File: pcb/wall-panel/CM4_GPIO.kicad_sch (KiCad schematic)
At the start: 24 parts, among them J10 THD-20-R, J15 THD-20-R, J16 Micro_SD_Card_Det, J18 THD-20-R, SW1 power reset, SW2 cpu reset, U10 RT9742GGJ5, U9 74LVC1G07SE-7

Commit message: wall panel v0.3
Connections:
- net ID_SC: now also JP4.1 (A); no longer JP4.3 (B)
- net ID_SD: now also JP3.1 (A); no longer JP3.3 (B)
- net SCL3: now also JP4.3 (B); no longer JP4.1 (A)
- net SDA3: now also JP3.3 (B); no longer JP3.1 (A)
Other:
- note added: "back plate"
- note added: "ethernet"
- company: Grigorii Merkushev (aka brushknight) -> dotstar.tech
- title: Wall panel -> Wall Panel
- moved on the sheet: JP3, JP4
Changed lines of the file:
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@@
 	(paper "A3")
 	(title_block
-		(title "Wall panel")
-		(date "2026-01-09")
-		(rev "1")
-		(company "Grigorii Merkushev (aka brushknight)")
-		(comment 1 "brushknight.com")
+		(title "Wall Panel")
+		(date "2026-02-02")
+		(rev "v0.3")
+		(company "dotstar.tech")
+		(comment 1 "designed by Grigorii Merkushev (aka brushknight)")
+		(comment 2 "brushknight.com")
 	)
 	(text "PWR LED"
@@
 		)
 	)
+	(text "back plate"
+		(exclude_from_sim no)
+		(at 254 21.082 0)
+		(effects
+			(font
+				(size 1.27 1.27)
+			)
+			(justify left bottom)
+		)
+	)
+	(text "ethernet"
+		(exclude_from_sim no)
+		(at 211.582 21.59 0)
+		(effects
+			(font
+				(size 1.27 1.27)
+			)
+			(justify left bottom)
+		)
+	)
 	(junction
 		(at 37.846 92.71)
@@
 	(wire
 		(pts
-			(xy 330.2 54.61) (xy 334.01 54.61)
+			(xy 327.66 72.39) (xy 331.47 72.39)
 		)
 		(stroke
@@
 	(wire
 		(pts
-			(xy 330.2 29.21) (xy 330.2 33.02)
+			(xy 327.66 46.99) (xy 327.66 50.8)
 		)
 		(stroke
@@
 	(wire
 		(pts
-			(xy 330.2 33.02) (xy 334.01 33.02)
+			(xy 327.66 50.8) (xy 331.47 50.8)
 		)
 		(stroke
@@
 	(wire
 		(pts
-			(xy 330.2 39.37) (xy 334.01 39.37)
+			(xy 327.66 57.15) (xy 331.47 57.15)
 		)
 		(stroke
@@
 	(wire
 		(pts
-			(xy 330.2 19.05) (xy 330.2 15.24)
+			(xy 327.66 36.83) (xy 327.66 33.02)
 		)
 		(stroke
@@
 	(wire
 		(pts
-			(xy 330.2 15.24) (xy 334.01 15.24)
+			(xy 327.66 33.02) (xy 331.47 33.02)
 		)
 		(stroke
@@
 	(wire
 		(pts
-			(xy 330.2 52.07) (xy 330.2 54.61)
+			(xy 327.66 69.85) (xy 327.66 72.39)
 		)
 		(stroke
@@
 	(wire
 		(pts
-			(xy 330.2 41.91) (xy 330.2 39.37)
+			(xy 327.66 59.69) (xy 327.66 57.15)
 		)
 		(stroke
@@
 	(hierarchical_label "SCL3"
 		(shape output)
-		(at 334.01 39.37 0)
+		(at 331.47 57.15 0)
 		(effects
 			(font
@@
 	(hierarchical_label "SDA3"
 		(shape output)
-		(at 334.01 15.24 0)
+		(at 331.47 33.02 0)
 		(effects
 			(font
@@
 	(hierarchical_label "TOUCH_SDA"
 		(shape output)
-		(at 334.01 24.13 0)
+		(at 331.47 41.91 0)
 		(effects
 			(font
@@
 	(hierarchical_label "TOUCH_SCL"
 		(shape output)
-		(at 334.01 46.99 0)
+		(at 331.47 64.77 0)
 		(effects
 			(font
@@
 	(hierarchical_label "ID_SD"
 		(shape output)
-		(at 334.01 33.02 0)
+		(at 331.47 50.8 0)
 		(effects
 			(font
@@
 	(hierarchical_label "ID_SC"
 		(shape output)
-		(at 334.01 54.61 0)
+		(at 331.47 72.39 0)
 		(effects
 			(font
@@
 		)
 		(instances
-			(project "CM4IOv5"
+			(project "wall_panel"
 				(path "/e63e39d7-6ac0-4ffd-8aa3-1841a4541b55/00000000-0000-0000-0000-00005cff706a"
 					(reference "#PWR078")
@@
 		)
 		(instances
-			(project "CM4IOv5"
+			(project "wall_panel"
 				(path "/e63e39d7-6ac0-4ffd-8aa3-1841a4541b55/00000000-0000-0000-0000-00005cff706a"
 					(reference "R24")
@@
 		)
 		(instances
-			(project "CM4IOv5"
+			(project "wall_panel"
 				(path "/e63e39d7-6ac0-4ffd-8aa3-1841a4541b55/00000000-0000-0000-0000-00005cff706a"
 					(reference "#PWR071")
@@
 		)
 		(instances
-			(project "CM4IOv5"
+			(project "wall_panel"
 				(path "/e63e39d7-6ac0-4ffd-8aa3-1841a4541b55/00000000-0000-0000-0000-00005cff706a"
 					(reference "#PWR032")
@@
 		)
 		(instances
-			(project "CM4IOv5"
+			(project "wall_panel"
 				(path "/e63e39d7-6ac0-4ffd-8aa3-1841a4541b55/00000000-0000-0000-0000-00005cff706a"
 					(reference "#PWR075")
@@
 		)
 		(instances
-			(project "CM4IOv5"
+			(project "wall_panel"
 				(path "/e63e39d7-6ac0-4ffd-8aa3-1841a4541b55/00000000-0000-0000-0000-00005cff706a"
 					(reference "#PWR045")
@@
 		)
 		(instances
-			(project "CM4IOv5"
+			(project "wall_panel"
 				(path "/e63e39d7-6ac0-4ffd-8aa3-1841a4541b55/00000000-0000-0000-0000-00005cff706a"
 					(reference "#PWR086")
@@
 		)
 		(instances
-			(project "CM4IOv5"
+			(project "wall_panel"
 				(path "/e63e39d7-6ac0-4ffd-8aa3-1841a4541b55/00000000-0000-0000-0000-00005cff706a"
 					(reference "#PWR073")
@@
 	(symbol
 		(lib_id "Jumper:SolderJumper_3_Bridged12")
-		(at 330.2 46.99 90)
-		(mirror x)
+		(at 327.66 64.77 90)
 		(unit 1)
 		(exclude_from_sim no)
@@
 		(dnp no)
 		(property "Reference" "JP4"
-			(at 327.66 48.2601 90)
+			(at 325.12 63.4999 90)
 			(effects
 				(font
@@
 		)
 		(property "Value" "GPIO reference"
-			(at 327.66 46.228 90)
+			(at 325.12 65.532 90)
 			(effects
 				(font
@@
 		)
 		(property "Footprint" "Jumper:SolderJumper-3_P1.3mm_Bridged12_RoundedPad1.0x1.5mm"
-			(at 330.2 46.99 0)
+			(at 327.66 64.77 0)
 			(effects
 				(font
@@
 		)
 		(property "Datasheet" "~"
-			(at 330.2 46.99 0)
+			(at 327.66 64.77 0)
 			(effects
 				(font
@@
 		)
 		(property "Description" "3-pole Solder Jumper, pins 1+2 closed/bridged"
-			(at 330.2 46.99 0)
+			(at 327.66 64.77 0)
 			(effects
 				(font
@@
 		)
 		(property "JLCPCB Rotation Offset" ""
-			(at 330.2 46.99 90)
+			(at 327.66 64.77 90)
 			(effects
 				(font
@@
 		)
 		(instances
-			(project "CM4IOv5"
+			(project "wall_panel"
 				(path "/e63e39d7-6ac0-4ffd-8aa3-1841a4541b55/00000000-0000-0000-0000-00005cff706a"
 					(reference "JP4")
@@
 		)
 		(instances
-			(project "CM4IOv5"
+			(project "wall_panel"
 				(path "/e63e39d7-6ac0-4ffd-8aa3-1841a4541b55/00000000-0000-0000-0000-00005cff706a"
 					(reference "J18")
@@
 		)
 		(instances
-			(project "CM4IOv5"
+			(project "wall_panel"
 				(path "/e63e39d7-6ac0-4ffd-8aa3-1841a4541b55/00000000-0000-0000-0000-00005cff706a"
 					(reference "#PWR077")
@@
 		)
 		(instances
-			(project "CM4IOv5"
+			(project "wall_panel"
 				(path "/e63e39d7-6ac0-4ffd-8aa3-1841a4541b55/00000000-0000-0000-0000-00005cff706a"
 					(reference "#PWR074")
@@
 	(symbol
 		(lib_id "Jumper:SolderJumper_3_Bridged12")
-		(at 330.2 24.13 90)
-		(mirror x)
+		(at 327.66 41.91 90)
 		(unit 1)
 		(exclude_from_sim no)
@@
 		(dnp no)
 		(property "Reference" "JP3"
-			(at 327.66 25.4001 90)
+			(at 325.12 40.6399 90)
 			(effects
 				(font
@@
 		)
 		(property "Value" "GPIO reference"
-			(at 327.66 23.368 90)
+			(at 325.12 42.672 90)
 			(effects
 				(font
@@
 		)
 		(property "Footprint" "Jumper:SolderJumper-3_P1.3mm_Bridged12_RoundedPad1.0x1.5mm"
-			(at 330.2 24.13 0)
+			(at 327.66 41.91 0)
 			(effects
 				(font
@@
 		)
 		(property "Datasheet" "~"
-			(at 330.2 24.13 0)
+			(at 327.66 41.91 0)
 			(effects
 				(font
@@
 		)
 		(property "Description" "3-pole Solder Jumper, pins 1+2 closed/bridged"
-			(at 330.2 24.13 0)
+			(at 327.66 41.91 0)
 			(effects
 				(font
@@
 		)
 		(property "JLCPCB Rotation Offset" ""
-			(at 330.2 24.13 90)
+			(at 327.66 41.91 90)
 			(effects
 				(font
@@
 		)
 		(instances
-			(project "CM4IOv5"
+			(project "wall_panel"
 				(path "/e63e39d7-6ac0-4ffd-8aa3-1841a4541b55/00000000-0000-0000-0000-00005cff706a"
 					(reference "JP3")
@@
 		)
 		(instances
-			(project "CM4IOv5"
+			(project "wall_panel"
 				(path "/e63e39d7-6ac0-4ffd-8aa3-1841a4541b55/00000000-0000-0000-0000-00005cff706a"
 					(reference "#PWR021")
@@
 		)
 		(instances
-			(project "CM4IOv5"
+			(project "wall_panel"
 				(path "/e63e39d7-6ac0-4ffd-8aa3-1841a4541b55/00000000-0000-0000-0000-00005cff706a"
 					(reference "S2")
@@
 		)
 		(instances
-			(project "CM4IOv5"
+			(project "wall_panel"
 				(path "/e63e39d7-6ac0-4ffd-8aa3-1841a4541b55/00000000-0000-0000-0000-00005cff706a"
 					(reference "SW2")
@@
 		)
 		(instances
-			(project "CM4IOv5"
+			(project "wall_panel"
 				(path "/e63e39d7-6ac0-4ffd-8aa3-1841a4541b55/00000000-0000-0000-0000-00005cff706a"
 					(reference "#PWR019")
@@
 		)
 		(instances
-			(project "CM4IOv5"
+			(project "wall_panel"
 				(path "/e63e39d7-6ac0-4ffd-8aa3-1841a4541b55/00000000-0000-0000-0000-00005cff706a"
 					(reference "#PWR080")
@@
 		)
 		(instances
-			(project "CM4IOv5"
+			(project "wall_panel"
 				(path "/e63e39d7-6ac0-4ffd-8aa3-1841a4541b55/00000000-0000-0000-0000-00005cff706a"
 					(reference "#PWR072")
@@
 		)
 		(instances
-			(project "CM4IOv5"
+			(project "wall_panel"
 				(path "/e63e39d7-6ac0-4ffd-8aa3-1841a4541b55/00000000-0000-0000-0000-00005cff706a"
 					(reference "#PWR085")
@@
 		)
 		(instances
-			(project "CM4IOv5"
+			(project "wall_panel"
 				(path "/e63e39d7-6ac0-4ffd-8aa3-1841a4541b55/00000000-0000-0000-0000-00005cff706a"
 					(reference "#PWR062")
@@
 		)
 		(instances
-			(project "CM4IOv5"
+			(project "wall_panel"
 				(path "/e63e39d7-6ac0-4ffd-8aa3-1841a4541b55/00000000-0000-0000-0000-00005cff706a"
 					(reference "J15")
@@
 		)
 		(instances
-			(project "CM4IOv5"
+			(project "wall_panel"
 				(path "/e63e39d7-6ac0-4ffd-8aa3-1841a4541b55/00000000-0000-0000-0000-00005cff706a"
 					(reference "#PWR076")

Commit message: small fixes of v0.3.1
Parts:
- added S3, S4, S5: SKSLLBE010, SKSLLBE010:SKSLLBE010, symbol SKSLLBE010:SKSLLBE010
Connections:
- net GND: now also S3.2, S4.2, S5.2
- net GPIO21: now also S3.1
- net GPIO26: now also S4.1, S5.1
- net nActivity_LED: now reaches Module1.21 (PI_nLED_Activity), R16.2
- net SDA5 renamed DISPLAY_PWM
- no-connect marks 9 -> 15
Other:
- note added: "Action Buttons"
- note added: "CM4 low speed"
- note added: "Headers"
- note added: "Pull Ups"
- note added: "Reset Buttons"
- note added: "Status LEDs"
- note added: "Touch BUS selector"
- note added: "VBUS"
- moved on the sheet: C31, D1, D2, J10, J15, J16, J18, JP1, JP3, JP4, Module1A, R16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

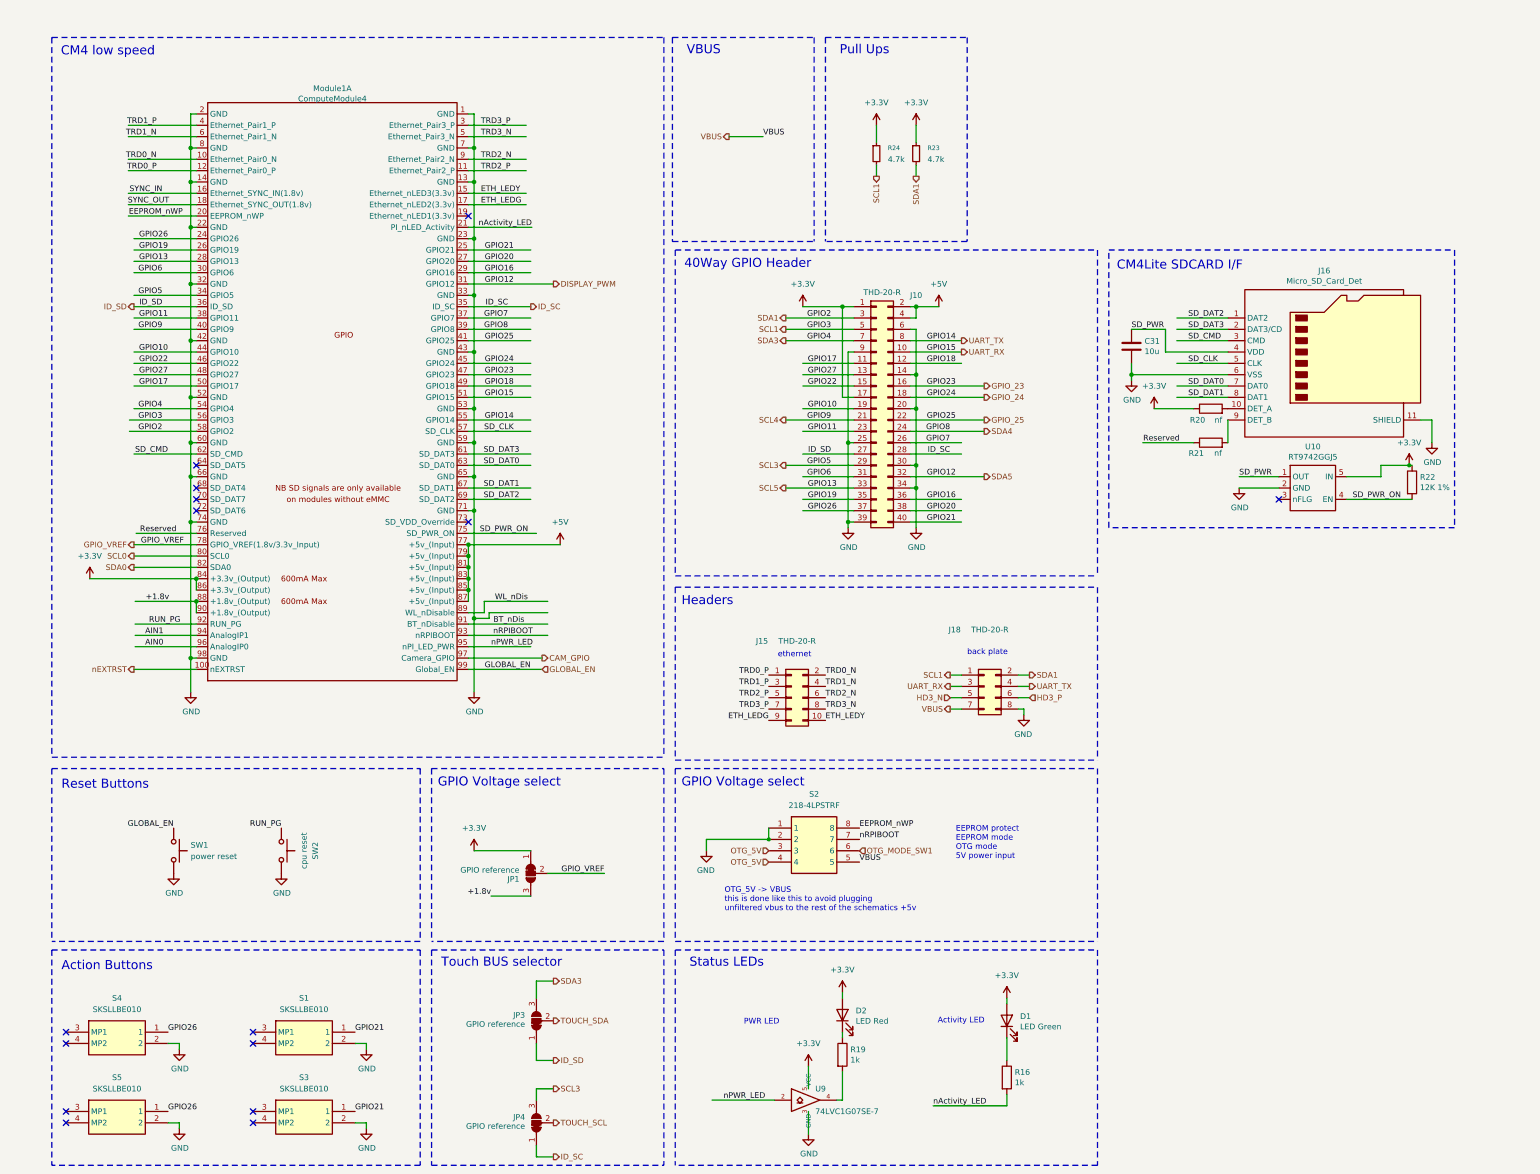
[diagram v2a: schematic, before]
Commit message: pogo pins wall panel
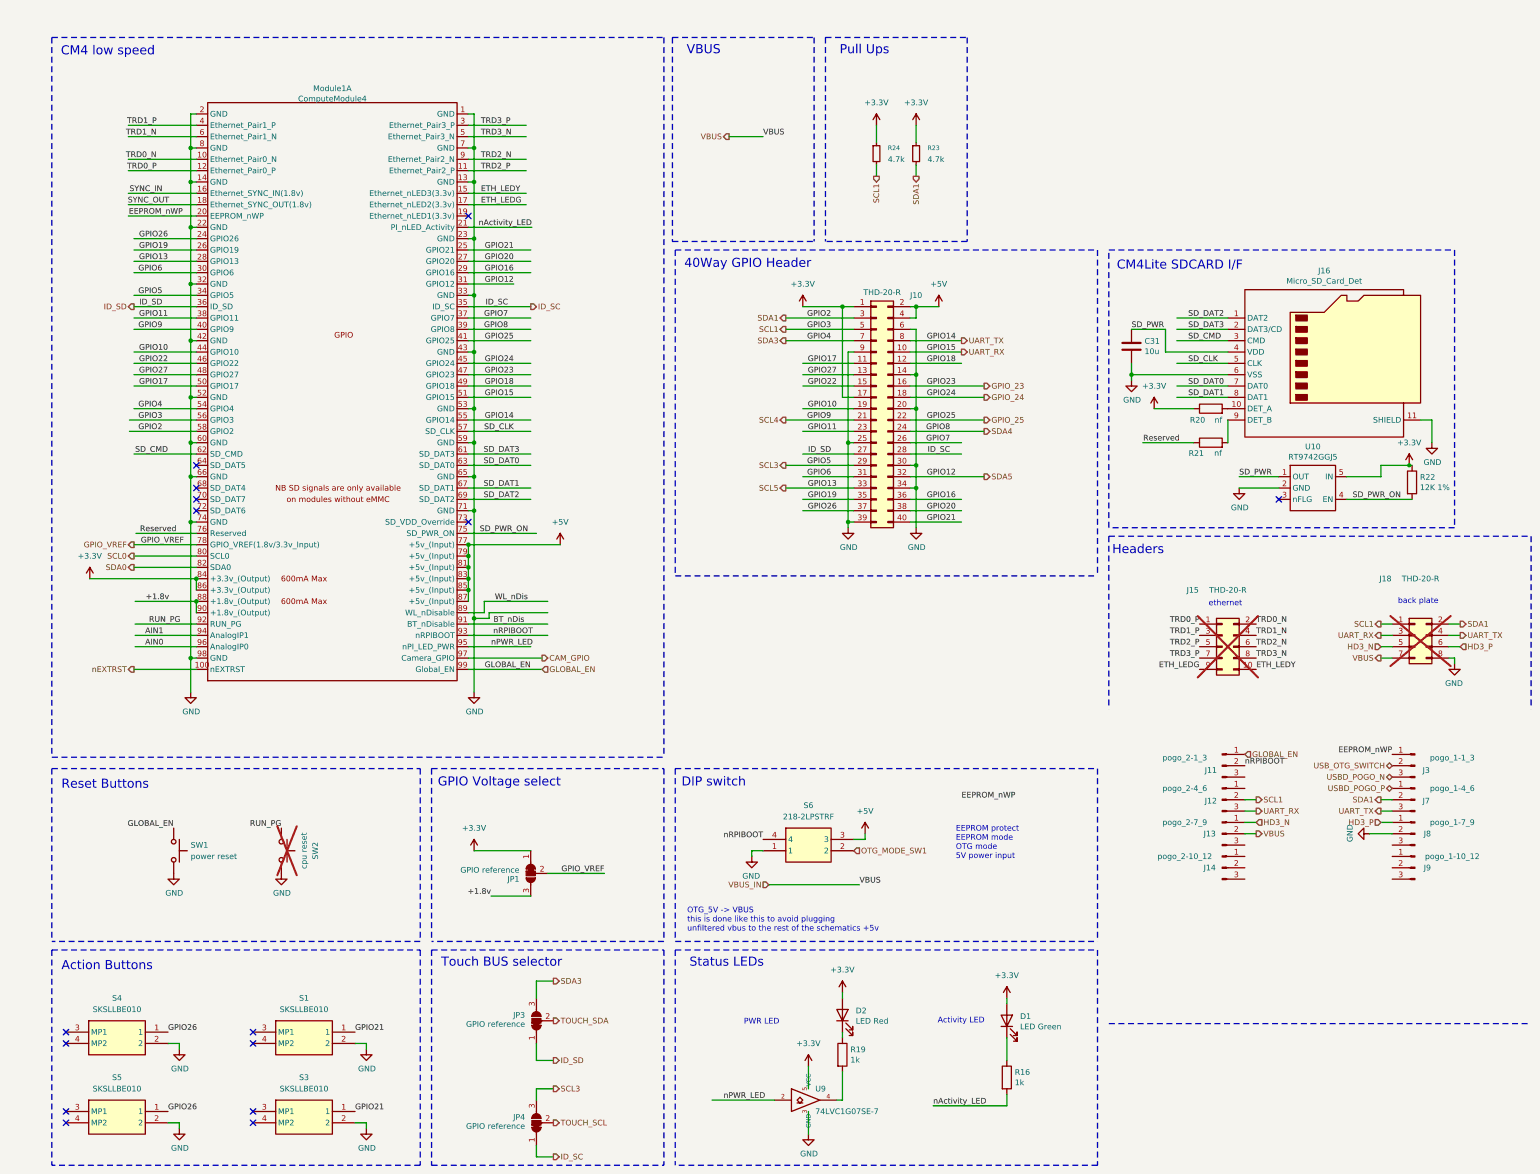
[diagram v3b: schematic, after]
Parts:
- removed S2: 218-4LPSTRF, 2184LPSTRF, symbol 218-4LPSTRF:218-4LPSTRF
- added J11: pogo_2-1_3, pogo:pogo_1x3, symbol Connector:Conn_01x03_Pin
- added J12: pogo_2-4_6, pogo:pogo_1x3, symbol Connector:Conn_01x03_Pin
- added J13: pogo_2-7_9, pogo:pogo_1x3, symbol Connector:Conn_01x03_Pin
- added J14: pogo_2-10_12, pogo:pogo_1x3, symbol Connector:Conn_01x03_Pin
- added J3: pogo_1-1_3, pogo:pogo_1x3, symbol Connector:Conn_01x03_Pin
- added J7: pogo_1-4_6, pogo:pogo_1x3, symbol Connector:Conn_01x03_Pin
- added J8: pogo_1-7_9, pogo:pogo_1x3, symbol Connector:Conn_01x03_Pin
- added J9: pogo_1-10_12, pogo:pogo_1x3, symbol Connector:Conn_01x03_Pin
- added S6: 218-2LPSTRF, 2182LPSTRF, symbol 218-2LPSTRF:218-2LPSTRF
- J15: now not fitted
- J18, SW2: now not fitted; now left out of the parts list
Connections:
- net +5V: now also S6.3
- net EEPROM_nWP: now also J3.1 (Pin_1)
- net GLOBAL_EN: now also J11.1 (Pin_1)
- net GND: now also J8.2 (Pin_2), S6.1
- net HD3_N: now also J13.1 (Pin_1)
- net HD3_P: now also J8.1 (Pin_1)
- net OTG_MODE_SW1: now also S6.2
- net SCL1: now also J12.2 (Pin_2)
- net SDA1: now also J7.2 (Pin_2)
- net UART_RX: now also J12.3 (Pin_3)
- net UART_TX: now also J7.3 (Pin_3)
- net VBUS: now also J13.2 (Pin_2)
- net nRPIBOOT: now also J11.2 (Pin_2), S6.4
- net DISPLAY_PWM renamed SDA5
- new net USBD_POGO_N: J3.3 (Pin_3)
- new net USBD_POGO_P: J7.1 (Pin_1)
- new net USB_OTG_SWITCH: J3.2 (Pin_2)
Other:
- note added: "DIP switch"
